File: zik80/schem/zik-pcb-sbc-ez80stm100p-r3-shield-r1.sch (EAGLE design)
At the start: 5 parts

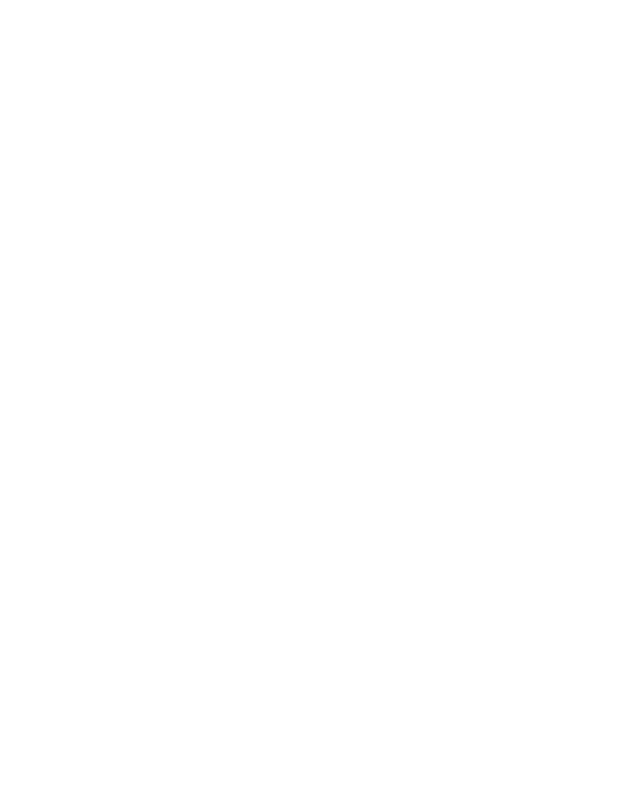
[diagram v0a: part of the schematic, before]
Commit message: Tweaking skeezix library for ZZ connectors
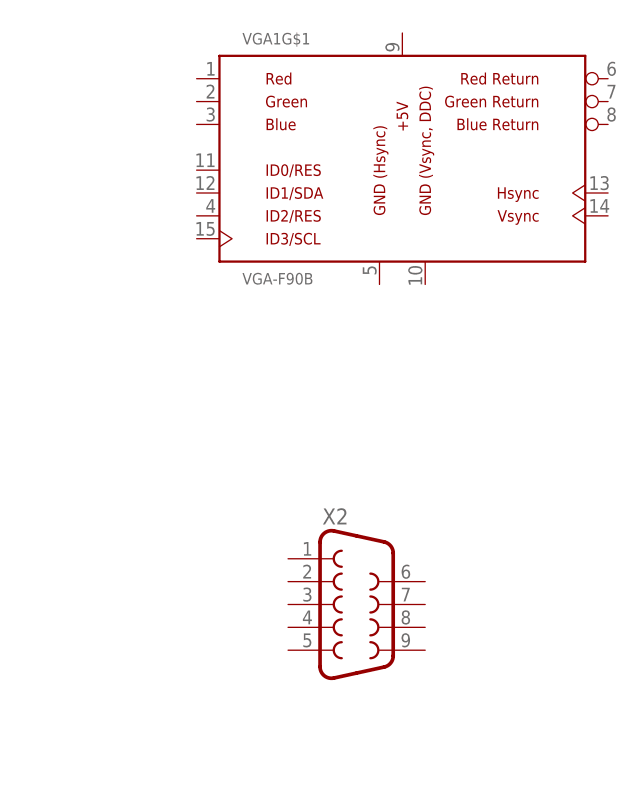
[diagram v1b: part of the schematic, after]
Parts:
- added VGA1: VGA-F90B, VideoConnectors:VGA-F90B
- added X2: (no value), SparkFun-Connectors-skeemod:DB9FEMALE
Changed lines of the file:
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@@
 <part name="U$3" library="skeezix" deviceset="POTWHEEL" device="" value="10K"/>
 <part name="U$4" library="SparkFun-Connectors-skeemod" deviceset="MINI-DIN6" device="PTH"/>
+<part name="VGA1" library="VideoConnectors" deviceset="VGA-*" device="F90B"/>
+<part name="X2" library="SparkFun-Connectors-skeemod" deviceset="DB9" device="FEMALE"/>
 </parts>
 <sheets>
@@
 <instance part="U$3" gate="G$1" x="73.66" y="55.88"/>
 <instance part="U$4" gate="G$1" x="88.9" y="27.94"/>
+<instance part="VGA1" gate="G$1" x="152.4" y="58.42"/>
+<instance part="X2" gate="G$1" x="147.32" y="10.16"/>
 </instances>
 <busses>

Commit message: Tweaking library some more
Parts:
- VGA1: device VideoConnectors:VGA-F90B -> VideoConnectors-skeemod:VGA-F90B
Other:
- moved on the sheet: VGA1G$1
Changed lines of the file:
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@@
 <part name="U$3" library="skeezix" deviceset="POTWHEEL" device="" value="10K"/>
 <part name="U$4" library="SparkFun-Connectors-skeemod" deviceset="MINI-DIN6" device="PTH"/>
-<part name="VGA1" library="VideoConnectors" deviceset="VGA-*" device="F90B"/>
 <part name="X2" library="SparkFun-Connectors-skeemod" deviceset="DB9" device="FEMALE"/>
+<part name="VGA1" library="VideoConnectors-skeemod" deviceset="VGA-*" device="F90B"/>
 </parts>
 <sheets>
@@
 <instance part="U$3" gate="G$1" x="73.66" y="55.88"/>
 <instance part="U$4" gate="G$1" x="88.9" y="27.94"/>
-<instance part="VGA1" gate="G$1" x="152.4" y="58.42"/>
 <instance part="X2" gate="G$1" x="147.32" y="10.16"/>
+<instance part="VGA1" gate="G$1" x="157.48" y="66.04"/>
 </instances>
 <busses>

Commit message: Tweaking libraries
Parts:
- X1: device adafruit-musb:USBMICRO_20329 -> adafruit-musb-skeemod:USBMICRO_20329
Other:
- moved on the sheet: X1
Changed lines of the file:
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@@
 <part name="U$1" library="skeezix" deviceset="DCJACKZIK" device=""/>
 <part name="U$2" library="skeezix" deviceset="MICROSD10" device=""/>
-<part name="X1" library="adafruit-musb" deviceset="USB" device="MICRO_20329"/>
 <part name="U$3" library="skeezix" deviceset="POTWHEEL" device="" value="10K"/>
 <part name="U$4" library="SparkFun-Connectors-skeemod" deviceset="MINI-DIN6" device="PTH"/>
 <part name="X2" library="SparkFun-Connectors-skeemod" deviceset="DB9" device="FEMALE"/>
 <part name="VGA1" library="VideoConnectors-skeemod" deviceset="VGA-*" device="F90B"/>
+<part name="X1" library="adafruit-musb-skeemod" deviceset="USB" device="MICRO_20329"/>
 </parts>
 <sheets>
@@
 <instance part="U$1" gate="G$1" x="30.48" y="30.48"/>
 <instance part="U$2" gate="G$1" x="30.48" y="-10.16"/>
-<instance part="X1" gate="G$1" x="43.18" y="63.5"/>
 <instance part="U$3" gate="G$1" x="73.66" y="55.88"/>
 <instance part="U$4" gate="G$1" x="88.9" y="27.94"/>
 <instance part="X2" gate="G$1" x="147.32" y="10.16"/>
 <instance part="VGA1" gate="G$1" x="157.48" y="66.04"/>
+<instance part="X1" gate="G$1" x="38.1" y="66.04"/>
 </instances>
 <busses>
